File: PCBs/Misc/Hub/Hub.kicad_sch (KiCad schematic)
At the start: 22 parts, among them J1 Conn_02x04_Top_Bottom, J2 Conn_02x04_Top_Bottom, U2 RJ45-B-1*4, U3 RJ45-B-1*4

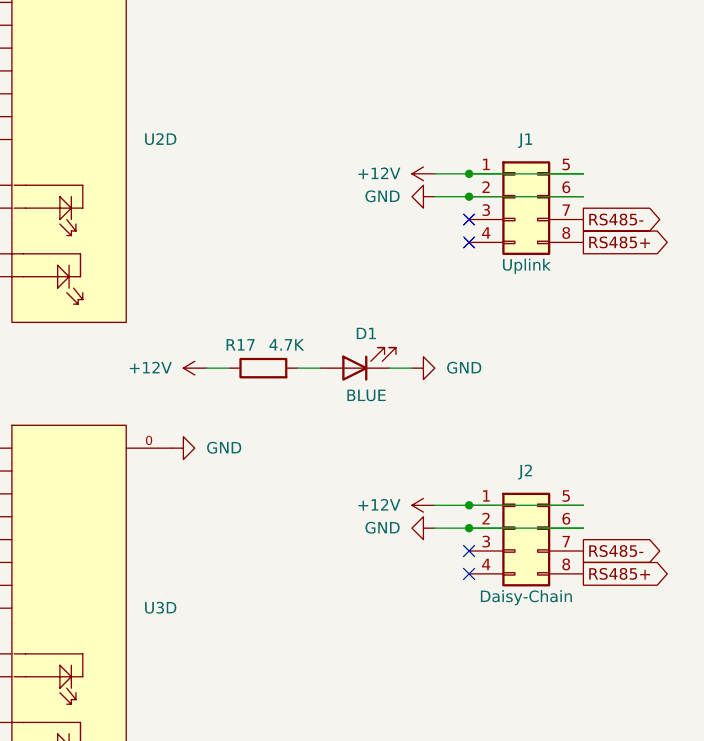
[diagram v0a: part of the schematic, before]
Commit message: Updated micro-fit pinout for more power
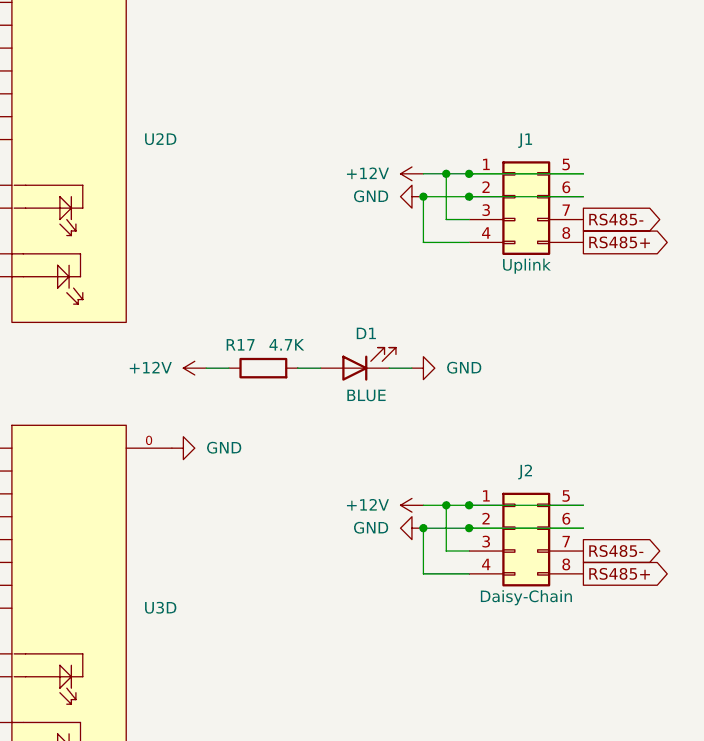
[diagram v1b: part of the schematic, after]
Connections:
- net +12V: now also J1.3 (Pin_3), J2.3 (Pin_3)
- net GND: now also J1.4 (Pin_4), J2.4 (Pin_4)
- no-connect marks 4 -> 0
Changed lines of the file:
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@@
 (kicad_sch (version 20211123) (generator eeschema)
   (paper "A4")
+  (junction (at 238.76 77.47) (diameter 0) (color 0 0 0 0)
+  )
+  (junction (at 238.76 114.3) (diameter 0) (color 0 0 0 0)
+  )
+  (junction (at 236.22 116.84) (diameter 0) (color 0 0 0 0)
+  )
   (junction (at 241.3 77.47) (diameter 0) (color 0 0 0 0)
   )
+  (junction (at 236.22 80.01) (diameter 0) (color 0 0 0 0)
+  )
   (junction (at 241.3 114.3) (diameter 0) (color 0 0 0 0)
   )
@@
   (junction (at 241.3 116.84) (diameter 0) (color 0 0 0 0)
   )
-  (no_connect (at 241.3 119.38))
-  (no_connect (at 241.3 82.55))
-  (no_connect (at 241.3 121.92))
-  (no_connect (at 241.3 85.09))
   (wire (pts (xy 241.3 77.47) (xy 254 77.47))
     (stroke (width 0) (type default) (color 0 0 0 0))
   )
-  (wire (pts (xy 237.49 77.47) (xy 241.3 77.47))
-    (stroke (width 0) (type default) (color 0 0 0 0))
-  )
-  (wire (pts (xy 237.49 114.3) (xy 241.3 114.3))
+  (wire (pts (xy 236.22 77.47) (xy 238.76 77.47))
+    (stroke (width 0) (type default) (color 0 0 0 0))
+  )
+  (wire (pts (xy 241.3 119.38) (xy 238.76 119.38))
+    (stroke (width 0) (type default) (color 0 0 0 0))
+  )
+  (wire (pts (xy 236.22 114.3) (xy 238.76 114.3))
+    (stroke (width 0) (type default) (color 0 0 0 0))
+  )
+  (wire (pts (xy 241.3 121.92) (xy 236.22 121.92))
+    (stroke (width 0) (type default) (color 0 0 0 0))
+  )
+  (wire (pts (xy 238.76 82.55) (xy 238.76 77.47))
+    (stroke (width 0) (type default) (color 0 0 0 0))
+  )
+  (wire (pts (xy 238.76 119.38) (xy 238.76 114.3))
     (stroke (width 0) (type default) (color 0 0 0 0))
   )
@@
     (stroke (width 0) (type default) (color 0 0 0 0))
   )
+  (wire (pts (xy 236.22 121.92) (xy 236.22 116.84))
+    (stroke (width 0) (type default) (color 0 0 0 0))
+  )
+  (wire (pts (xy 241.3 85.09) (xy 236.22 85.09))
+    (stroke (width 0) (type default) (color 0 0 0 0))
+  )
   (wire (pts (xy 241.3 116.84) (xy 254 116.84))
     (stroke (width 0) (type default) (color 0 0 0 0))
   )
+  (wire (pts (xy 241.3 82.55) (xy 238.76 82.55))
+    (stroke (width 0) (type default) (color 0 0 0 0))
+  )
   (wire (pts (xy 241.3 80.01) (xy 254 80.01))
     (stroke (width 0) (type default) (color 0 0 0 0))
@@
     (stroke (width 0) (type default) (color 0 0 0 0))
   )
-  (wire (pts (xy 237.49 116.84) (xy 241.3 116.84))
-    (stroke (width 0) (type default) (color 0 0 0 0))
-  )
-  (wire (pts (xy 237.49 80.01) (xy 241.3 80.01))
+  (wire (pts (xy 236.22 85.09) (xy 236.22 80.01))
+    (stroke (width 0) (type default) (color 0 0 0 0))
+  )
+  (wire (pts (xy 238.76 77.47) (xy 241.3 77.47))
+    (stroke (width 0) (type default) (color 0 0 0 0))
+  )
+  (wire (pts (xy 236.22 116.84) (xy 241.3 116.84))
+    (stroke (width 0) (type default) (color 0 0 0 0))
+  )
+  (wire (pts (xy 238.76 114.3) (xy 241.3 114.3))
+    (stroke (width 0) (type default) (color 0 0 0 0))
+  )
+  (wire (pts (xy 236.22 80.01) (xy 241.3 80.01))
     (stroke (width 0) (type default) (color 0 0 0 0))
   )
@@
     (pin "1")
   )
-  (symbol (lib_id "power:GND") (at 237.49 116.84 270) (unit 1)
-    (in_bom yes) (on_board yes) (fields_autoplaced)
-    (property "Reference" "#PWR0111" (id 0) (at 231.14 116.84 0)
-      (effects (font (size 1.27 1.27)) hide)
-    )
-    (property "Value" "GND" (id 1) (at 233.68 116.8399 90)
-      (effects (font (size 1.27 1.27)) (justify right))
-    )
-    (property "Footprint" "" (id 2) (at 237.49 116.84 0)
-      (effects (font (size 1.27 1.27)) hide)
-    )
-    (property "Datasheet" "" (id 3) (at 237.49 116.84 0)
+  (symbol (lib_id "power:GND") (at 236.22 116.84 270) (unit 1)
+    (in_bom yes) (on_board yes) (fields_autoplaced)
+    (property "Reference" "#PWR0111" (id 0) (at 229.87 116.84 0)
+      (effects (font (size 1.27 1.27)) hide)
+    )
+    (property "Value" "GND" (id 1) (at 232.41 116.8399 90)
+      (effects (font (size 1.27 1.27)) (justify right))
+    )
+    (property "Footprint" "" (id 2) (at 236.22 116.84 0)
+      (effects (font (size 1.27 1.27)) hide)
+    )
+    (property "Datasheet" "" (id 3) (at 236.22 116.84 0)
       (effects (font (size 1.27 1.27)) hide)
     )
@@
     (pin "48")
   )
-  (symbol (lib_id "power:GND") (at 237.49 80.01 270) (unit 1)
-    (in_bom yes) (on_board yes) (fields_autoplaced)
-    (property "Reference" "#PWR0110" (id 0) (at 231.14 80.01 0)
-      (effects (font (size 1.27 1.27)) hide)
-    )
-    (property "Value" "GND" (id 1) (at 233.68 80.0099 90)
-      (effects (font (size 1.27 1.27)) (justify right))
-    )
-    (property "Footprint" "" (id 2) (at 237.49 80.01 0)
-      (effects (font (size 1.27 1.27)) hide)
-    )
-    (property "Datasheet" "" (id 3) (at 237.49 80.01 0)
+  (symbol (lib_id "power:GND") (at 236.22 80.01 270) (unit 1)
+    (in_bom yes) (on_board yes) (fields_autoplaced)
+    (property "Reference" "#PWR0110" (id 0) (at 229.87 80.01 0)
+      (effects (font (size 1.27 1.27)) hide)
+    )
+    (property "Value" "GND" (id 1) (at 232.41 80.0099 90)
+      (effects (font (size 1.27 1.27)) (justify right))
+    )
+    (property "Footprint" "" (id 2) (at 236.22 80.01 0)
+      (effects (font (size 1.27 1.27)) hide)
+    )
+    (property "Datasheet" "" (id 3) (at 236.22 80.01 0)
       (effects (font (size 1.27 1.27)) hide)
     )
@@
     (pin "1")
   )
-  (symbol (lib_id "power:+12V") (at 237.49 77.47 90) (unit 1)
-    (in_bom yes) (on_board yes) (fields_autoplaced)
-    (property "Reference" "#PWR0109" (id 0) (at 241.3 77.47 0)
-      (effects (font (size 1.27 1.27)) hide)
-    )
-    (property "Value" "+12V" (id 1) (at 233.68 77.4699 90)
-      (effects (font (size 1.27 1.27)) (justify left))
-    )
-    (property "Footprint" "" (id 2) (at 237.49 77.47 0)
-      (effects (font (size 1.27 1.27)) hide)
-    )
-    (property "Datasheet" "" (id 3) (at 237.49 77.47 0)
+  (symbol (lib_id "power:+12V") (at 236.22 77.47 90) (unit 1)
+    (in_bom yes) (on_board yes) (fields_autoplaced)
+    (property "Reference" "#PWR0109" (id 0) (at 240.03 77.47 0)
+      (effects (font (size 1.27 1.27)) hide)
+    )
+    (property "Value" "+12V" (id 1) (at 232.41 77.4699 90)
+      (effects (font (size 1.27 1.27)) (justify left))
+    )
+    (property "Footprint" "" (id 2) (at 236.22 77.47 0)
+      (effects (font (size 1.27 1.27)) hide)
+    )
+    (property "Datasheet" "" (id 3) (at 236.22 77.47 0)
       (effects (font (size 1.27 1.27)) hide)
     )
@@
     (pin "2")
   )
-  (symbol (lib_id "power:+12V") (at 237.49 114.3 90) (unit 1)
-    (in_bom yes) (on_board yes) (fields_autoplaced)
-    (property "Reference" "#PWR0112" (id 0) (at 241.3 114.3 0)
-      (effects (font (size 1.27 1.27)) hide)
-    )
-    (property "Value" "+12V" (id 1) (at 233.68 114.2999 90)
-      (effects (font (size 1.27 1.27)) (justify left))
-    )
-    (property "Footprint" "" (id 2) (at 237.49 114.3 0)
-      (effects (font (size 1.27 1.27)) hide)
-    )
-    (property "Datasheet" "" (id 3) (at 237.49 114.3 0)
-      (effects (font (size 1.27 1.27)) hide)
-    )
+  (symbol (lib_id "power:+12V") (at 236.22 114.3 90) (unit 1)
+    (in_bom yes) (on_board yes) (fields_autoplaced)
+    (property "Reference" "#PWR0112" (id 0) (at 240.03 114.3 0)
+      (effects (font (size 1.27 1.27)) hide)
+    )
+    (property "Value" "+12V" (id 1) (at 232.41 114.2999 90)
+      (effects (font (size 1.27 1.27)) (justify left))
+    )
+    (property "Footprint" "" (id 2) (at 236.22 114.3 0)
+      (effects (font (size 1.27 1.27)) hide)
+    )
+    (property "Datasheet" "" (id 3) (at 236.22 114.3 0)
+      (effects (font (size 1.27 1.27)) hide)
+    )

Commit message: Tweaked Hub
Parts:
- removed R1, R10, R11, R12, R13, R14, R15, R16, R2, R3, R4, R5, R6, R7, R8, R9: 1.8K, A10 KiCad Libraries:R0805, symbol Device:R
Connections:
- net +12V: now also U2.14, U2.2, U2.26, U2.38, U3.14, U3.2, U3.26, U3.38
- net GND: now also U2.1, U2.13, U2.25, U2.37, U3.1, U3.13, U3.25, U3.37
- net RX_LED1: no longer names the net of U2.12
- net RX_LED1: no longer U2.2
- net RX_LED2: no longer names the net of U2.24
- net RX_LED2: no longer U2.14
- net RX_LED3: no longer names the net of U2.36
- net RX_LED3: no longer U2.26
- net RX_LED4: no longer names the net of U2.48
- net RX_LED4: no longer U2.38
- net RX_LED5: no longer names the net of U3.12
- net RX_LED5: no longer U3.2
- net RX_LED6: no longer names the net of U3.24
- net RX_LED6: no longer U3.14
- net RX_LED7: no longer names the net of U3.36
- net RX_LED7: no longer U3.26
- net RX_LED8: no longer names the net of U3.48
- net RX_LED8: no longer U3.38
- net TX_LED1: no longer names the net of U2.10
- net TX_LED1: no longer U2.1
- net TX_LED2: no longer names the net of U2.22
- net TX_LED2: no longer U2.13
- net TX_LED3: no longer names the net of U2.34
- net TX_LED3: no longer U2.25
- net TX_LED4: no longer names the net of U2.46
- net TX_LED4: no longer U2.37
- net TX_LED5: no longer names the net of U3.10
- net TX_LED5: no longer U3.1
- net TX_LED6: no longer names the net of U3.22
- net TX_LED6: no longer U3.13
- net TX_LED7: no longer names the net of U3.34
- net TX_LED7: no longer U3.25
- net TX_LED8: no longer names the net of U3.46
- net TX_LED8: no longer U3.37
- no-connect marks 0 -> 32

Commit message: Updated HUB
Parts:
- removed U2, U3: RJ45-B-1*4, A10 KiCad Libraries:RJ45-TH_B-1-4, symbol A10:RJ45-B-1*4
- added RJ1: DS1130-S80BP, A10 KiCad Libraries:RJ45-TH_DS1130-S80BP, symbol A10:DS1130-S80BP
- J1, J2: LCSC C234189 -> C122422; now in the parts list
- R1: renamed from R17; footprint A10 KiCad Libraries:R0805 -> Resistor_SMD:R_0603_1608Metric; LCSC C17673 -> C23162
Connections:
- net +12V: now also RJ1.12, RJ1.13, RJ1.15, RJ1.20, RJ1.21, RJ1.23, RJ1.28, RJ1.29, RJ1.31, RJ1.36, RJ1.37, RJ1.39, RJ1.4, RJ1.44, RJ1.45, RJ1.47, RJ1.5, RJ1.52, RJ1.53, RJ1.55, RJ1.60, RJ1.61, RJ1.63, RJ1.7
- net GND: now also RJ1.0, RJ1.1, RJ1.10, RJ1.16, RJ1.17, RJ1.18, RJ1.2, RJ1.24, RJ1.25, RJ1.26, RJ1.32, RJ1.33, RJ1.34, RJ1.40, RJ1.41, RJ1.42, RJ1.48, RJ1.49, RJ1.50, RJ1.56, RJ1.57, RJ1.58, RJ1.64, RJ1.8, RJ1.9
- net RS485+: now also RJ1.14, RJ1.22, RJ1.30, RJ1.38, RJ1.46, RJ1.54, RJ1.6, RJ1.62
- net RS485-: now also RJ1.11, RJ1.19, RJ1.27, RJ1.3, RJ1.35, RJ1.43, RJ1.51, RJ1.59
- no-connect marks 32 -> 0
